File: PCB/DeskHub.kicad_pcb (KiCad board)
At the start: 4 copper layers, 212.6 x 108.9 mm, 120 parts, among them J1 USB_A, J2 5V Barrel, J4 USB_A, J5 USB_A, J6 USB_A, J7 USB_A, U1 TUSB4041I, U2 3.3V Reg, U3 1.1V Reg, U4 TPS2001CDGNR, U5 TPS2001CDGNR, U6 TPS2001CDGNR, U7 TPS2001CDGNR, Y1 ECS-240-20-30B-TR

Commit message: space out vias, add stiching vias, remove teardrops
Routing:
- net BOARD_3.3V: track 4.62 -> 7.07 mm, vias 42 -> 23
- net /Port 3 Power Switch/OVERCURRENT: track 80.4 -> 79.7 mm
- net VDD3.3: vias 16 -> 8
- net VDD1.1: vias 19 -> 11
- net Earth: vias 53 -> 99
- net BOARD_5V: vias 36 -> 29
- net /Port 4 Power Switch/VOUT: vias 4 -> 2
- net /Port 3 Power Switch/VOUT: vias 4 -> 2
- net /Port 2 Power Switch/VOUT: vias 4 -> 2
- net /Port 1 Power Switch/VOUT: vias 4 -> 2
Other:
- board text added: "10K 4.7K ..."

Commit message: pcb v2.0 condensed
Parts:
- moved J6 61.8 mm to (187.5, 137.0)
- moved C69 61.8 mm to (199.3, 132.8)
- moved C70 61.8 mm to (198.4, 132.8)
- moved R18 61.8 mm to (197.4, 132.8)
- moved C42 58.7 mm to (187.1, 78.0)
- moved J7 56.3 mm to (123.5, 137.0)
- moved FB7 55.1 mm to (115.3, 127.7)
- moved C74 54.9 mm to (118.1, 128.1), turned to 90 degrees
- moved C49 54.4 mm to (117.0, 117.2)
- moved R11 54.2 mm to (118.0, 119.6)
- moved C48 54.2 mm to (116.7, 125.3)
- moved U4 54.2 mm to (114.5, 121.3)
- moved C71 54.0 mm to (184.0, 128.1)
- moved FB4 53.8 mm to (182.1, 127.8)
- moved J2 53.8 mm to (197.7, 67.2)
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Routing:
- net USB_DN4_D+: track 146.3 -> 65.1 mm
- net USB_DN4_D-: track 146.2 -> 65.1 mm
- net /Port 4 Power Switch/PWRON_EN: track 130.6 -> 65.2 mm
- net /Port 1 Power Switch/OVERCURRENT: track 125.0 -> 60.8 mm
- net /Port 1 Power Switch/PWRON_EN: track 142.3 -> 78.8 mm
- net /Port 4 Power Switch/OVERCURRENT: track 121.4 -> 59.0 mm
- net USB_DN1_D-: track 111.1 -> 63.9 mm
- net USB_DN1_D+: track 111.1 -> 63.9 mm
- net USB_DN3_D-: track 96.7 -> 53.2 mm
- net USB_DN3_D+: track 96.7 -> 53.2 mm
- net /Port 2 Power Switch/OVERCURRENT: track 85.9 -> 48.3 mm
- net /Port 3 Power Switch/PWRON_EN: track 91.9 -> 55.3 mm
- net /Port 3 Power Switch/OVERCURRENT: track 79.7 -> 43.2 mm
- net /Port 2 Power Switch/PWRON_EN: track 98.9 -> 62.4 mm
- net USB_DN2_D-: track 81.8 -> 57.6 mm
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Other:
- board size 212.6 x 108.9 mm -> 94 x 84.2 mm

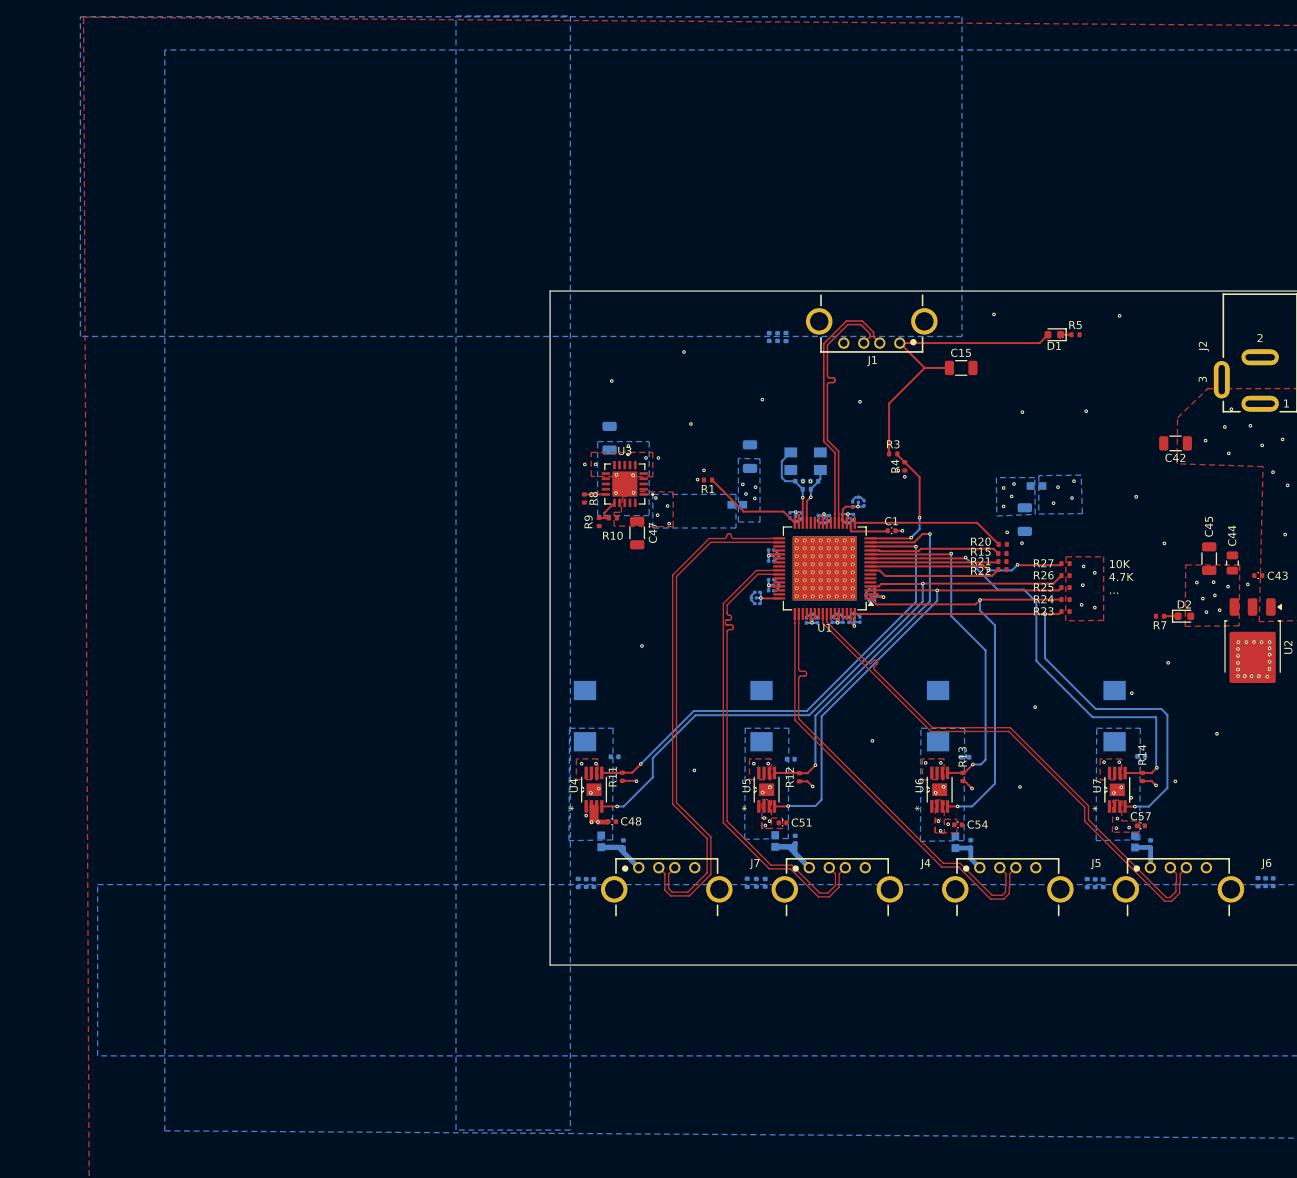
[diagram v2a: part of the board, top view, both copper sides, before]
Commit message: pcb v2.01 reddit review post
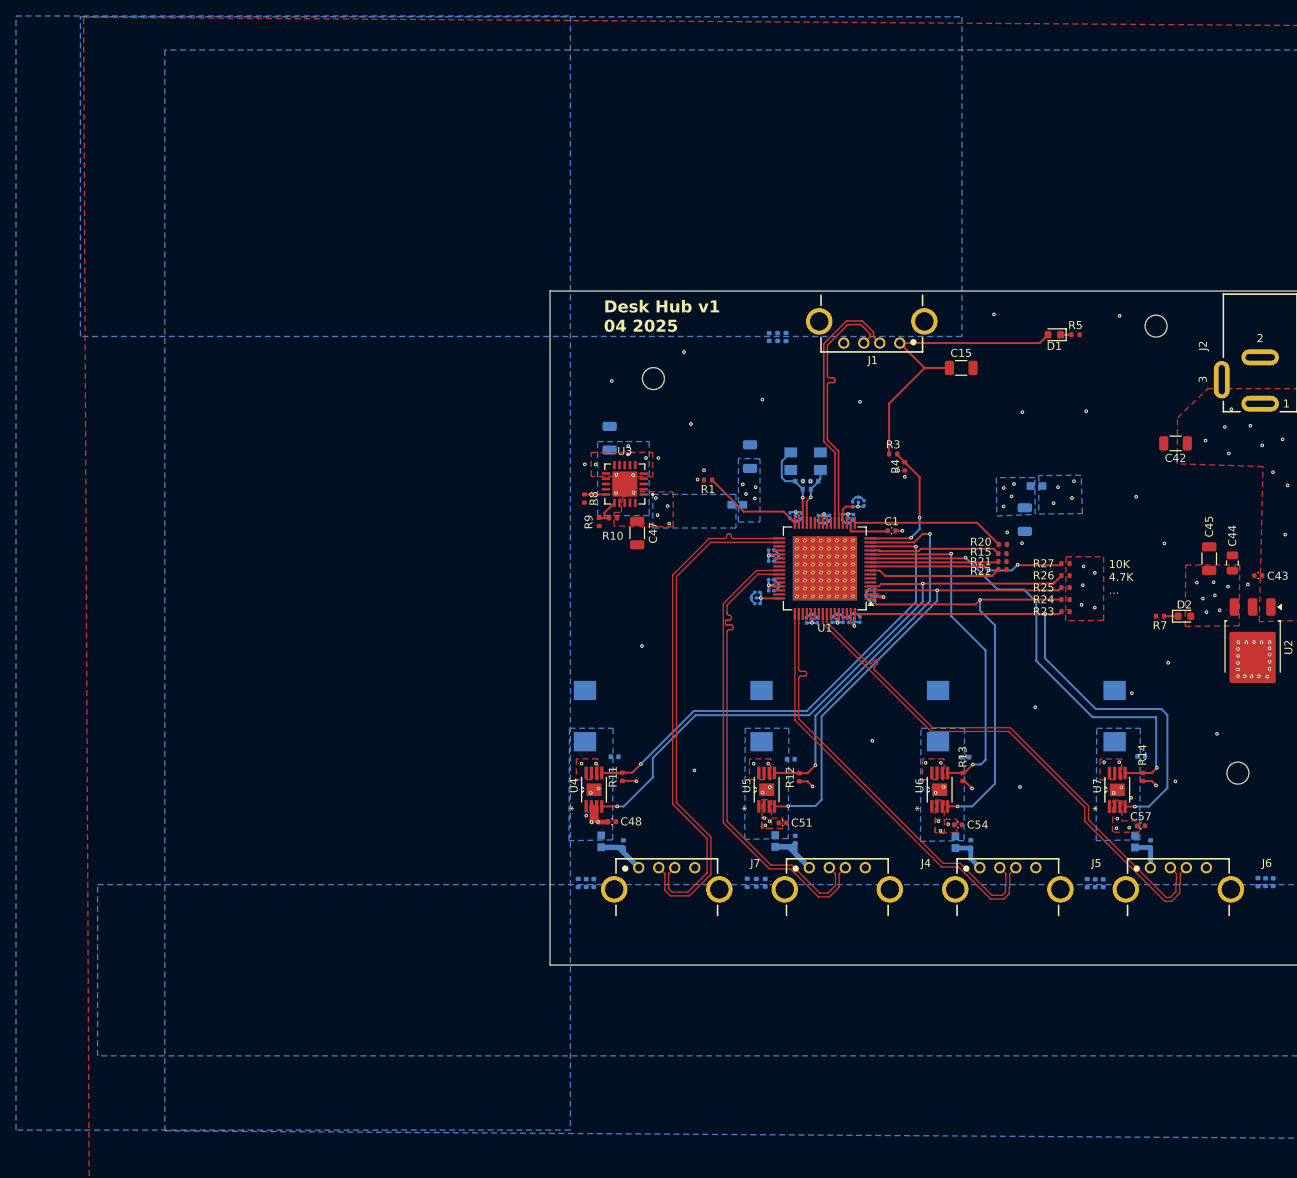
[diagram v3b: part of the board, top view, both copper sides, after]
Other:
- outline, holes or cut-outs redrawn
- board text added: "Desk Hub v1 04 2025"
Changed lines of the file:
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@@
 			(crossoutdnponfab yes)
 			(subtractmaskfromsilk no)
-			(outputformat 1)
+			(outputformat 4)
 			(mirror no)
-			(drillshape 1)
+			(drillshape 0)
 			(scaleselection 1)
 			(outputdirectory "")
@@
 		)
 		(property "Value" "5V Barrel"
-			(at 4.195 12.24 270)
+			(at -2.74 9.395 270)
 			(layer "F.Fab")
 			(effects
@@
 		)
 		(property "Value" "1.1V Reg"
-			(at 9.835 3.885 0)
+			(at 4.55 5.15 0)
 			(layer "F.Fab")
 			(effects
@@
 		(layer "B.SilkS")
 	)
+	(gr_circle
+		(center 121.875 69.875)
+		(end 123.25 69.875)
+		(stroke
+			(width 0.1)
+			(type solid)
+		)
+		(fill no)
+		(layer "Edge.Cuts")
+	)
+	(gr_circle
+		(center 184.714513 63.314514)
+		(end 186.089513 63.314514)
+		(stroke
+			(width 0.1)
+			(type solid)
+		)
+		(fill no)
+		(layer "Edge.Cuts")
+	)
+	(gr_circle
+		(center 194.939513 119.189514)
+		(end 196.314513 119.189514)
+		(stroke
+			(width 0.1)
+			(type solid)
+		)
+		(fill no)
+		(layer "Edge.Cuts")
+	)
 	(gr_rect
 		(start 108.965 58.93)
@@
 		)
 	)
+	(gr_text "Desk Hub v1\n04 2025"
+		(at 115.675 64.2 0)
+		(layer "F.SilkS")
+		(effects
+			(font
+				(size 1.5 1.5)
+				(thickness 0.3)
+				(bold yes)
+			)
+			(justify left bottom)
+		)
+	)
 	(segment
 		(start 152.13 88.9)
@@
 	)
 	(zone
+		(net 0)
+		(net_name "")
+		(layers "F.Cu" "B.Cu" "In1.Cu" "In2.Cu")
+		(name "Keep Out")
+		(hatch edge 0.5)
+		(connect_pads
+			(clearance 0)
+		)
+		(min_thickness 0.25)
+		(filled_areas_thickness no)
+		(keepout
+			(tracks not_allowed)
+			(vias not_allowed)
+			(pads not_allowed)
+			(copperpour not_allowed)
+			(footprints not_allowed)
+		)
+		(placement
+			(enabled no)
+			(sheetname "/")
+		)
+		(fill
+			(thermal_gap 0.5)
+			(thermal_bridge_width 0.5)
+		)
+		(polygon
+			(pts
+				(xy 186.585498 63.191883) (xy 186.553485 62.94872) (xy 186.490007 62.711815) (xy 186.396149 62.485223)
+				(xy 186.273519 62.27282) (xy 186.124213 62.078241) (xy 185.950786 61.904814) (xy 185.756207 61.755508)
+				(xy 185.543804 61.632878) (xy 185.317212 61.53902) (xy 185.080307 61.475542) (xy 184.837144 61.443529)
+				(xy 184.591882 61.443529) (xy 184.348719 61.475542) (xy 184.111814 61.53902) (xy 183.885222 61.632878)
+				(xy 183.672819 61.755508) (xy 183.47824 61.904814) (xy 183.304813 62.078241) (xy 183.155507 62.27282)
+				(xy 183.032877 62.485223) (xy 182.939019 62.711815) (xy 182.875541 62.94872) (xy 182.843528 63.191883)
+				(xy 182.843528 63.437145) (xy 182.875541 63.680308) (xy 182.939019 63.917213) (xy 183.032877 64.143805)
+				(xy 183.155507 64.356208) (xy 183.304813 64.550787) (xy 183.47824 64.724214) (xy 183.672819 64.87352)
+				(xy 183.885222 64.99615) (xy 184.111814 65.090008) (xy 184.348719 65.153486) (xy 184.591882 65.185499)
+				(xy 184.837144 65.185499) (xy 185.080307 65.153486) (xy 185.317212 65.090008) (xy 185.543804 64.99615)
+				(xy 185.756207 64.87352) (xy 185.950786 64.724214) (xy 186.124213 64.550787) (xy 186.273519 64.356208)
+				(xy 186.396149 64.143805) (xy 186.490007 63.917213) (xy 186.553485 63.680308) (xy 186.585498 63.437145)
+			)
+		)
+	)
+	(zone
+		(net 0)
+		(net_name "")
+		(layers "F.Cu" "B.Cu" "In1.Cu" "In2.Cu")
+		(name "Keep Out")
+		(hatch edge 0.5)
+		(connect_pads
+			(clearance 0)
+		)
+		(min_thickness 0.25)
+		(filled_areas_thickness no)
+		(keepout
+			(tracks not_allowed)
+			(vias not_allowed)
+			(pads not_allowed)
+			(copperpour not_allowed)
+			(footprints not_allowed)
+		)
+		(placement
+			(enabled no)
+			(sheetname "/")
+		)
+		(fill
+			(thermal_gap 0.5)
+			(thermal_bridge_width 0.5)
+		)
+		(polygon
+			(pts
+				(xy 123.745985 69.752369) (xy 123.713972 69.509206) (xy 123.650494 69.272301) (xy 123.556636 69.045709)
+				(xy 123.434006 68.833306) (xy 123.2847 68.638727) (xy 123.111273 68.4653) (xy 122.916694 68.315994)
+				(xy 122.704291 68.193364) (xy 122.477699 68.099506) (xy 122.240794 68.036028) (xy 121.997631 68.004015)
+				(xy 121.752369 68.004015) (xy 121.509206 68.036028) (xy 121.272301 68.099506) (xy 121.045709 68.193364)
+				(xy 120.833306 68.315994) (xy 120.638727 68.4653) (xy 120.4653 68.638727) (xy 120.315994 68.833306)
+				(xy 120.193364 69.045709) (xy 120.099506 69.272301) (xy 120.036028 69.509206) (xy 120.004015 69.752369)
+				(xy 120.004015 69.997631) (xy 120.036028 70.240794) (xy 120.099506 70.477699) (xy 120.193364 70.704291)
+				(xy 120.315994 70.916694) (xy 120.4653 71.111273) (xy 120.638727 71.2847) (xy 120.833306 71.434006)
+				(xy 121.045709 71.556636) (xy 121.272301 71.650494) (xy 121.509206 71.713972) (xy 121.752369 71.745985)
+				(xy 121.997631 71.745985) (xy 122.240794 71.713972) (xy 122.477699 71.650494) (xy 122.704291 71.556636)
+				(xy 122.916694 71.434006) (xy 123.111273 71.2847) (xy 123.2847 71.111273) (xy 123.434006 70.916694)
+				(xy 123.556636 70.704291) (xy 123.650494 70.477699) (xy 123.713972 70.240794) (xy 123.745985 69.997631)
+			)
+		)
+	)
+	(zone
+		(net 0)
+		(net_name "")
+		(layers "F.Cu" "B.Cu" "In1.Cu" "In2.Cu")
+		(name "Keep Out")
+		(hatch edge 0.5)
+		(connect_pads
+			(clearance 0)
+		)
+		(min_thickness 0.25)
+		(filled_areas_thickness no)
+		(keepout
+			(tracks not_allowed)
+			(vias not_allowed)
+			(pads not_allowed)
+			(copperpour not_allowed)
+			(footprints not_allowed)
+		)
+		(placement
+			(enabled no)
+			(sheetname "/")
+		)
+		(fill
+			(thermal_gap 0.5)
+			(thermal_bridge_width 0.5)
+		)
+		(polygon
+			(pts
+				(xy 196.810498 119.066883) (xy 196.778485 118.82372) (xy 196.715007 118.586815) (xy 196.621149 118.360223)
+				(xy 196.498519 118.14782) (xy 196.349213 117.953241) (xy 196.175786 117.779814) (xy 195.981207 117.630508)
+				(xy 195.768804 117.507878) (xy 195.542212 117.41402) (xy 195.305307 117.350542) (xy 195.062144 117.318529)
+				(xy 194.816882 117.318529) (xy 194.573719 117.350542) (xy 194.336814 117.41402) (xy 194.110222 117.507878)
+				(xy 193.897819 117.630508) (xy 193.70324 117.779814) (xy 193.529813 117.953241) (xy 193.380507 118.14782)
+				(xy 193.257877 118.360223) (xy 193.164019 118.586815) (xy 193.100541 118.82372) (xy 193.068528 119.066883)
+				(xy 193.068528 119.312145) (xy 193.100541 119.555308) (xy 193.164019 119.792213) (xy 193.257877 120.018805)
+				(xy 193.380507 120.231208) (xy 193.529813 120.425787) (xy 193.70324 120.599214) (xy 193.897819 120.74852)
+				(xy 194.110222 120.87115) (xy 194.336814 120.965008) (xy 194.573719 121.028486) (xy 194.816882 121.060499)
+				(xy 195.062144 121.060499) (xy 195.305307 121.028486) (xy 195.542212 120.965008) (xy 195.768804 120.87115)
+				(xy 195.981207 120.74852) (xy 196.175786 120.599214) (xy 196.349213 120.425787) (xy 196.498519 120.231208)
+				(xy 196.621149 120.018805) (xy 196.715007 119.792213) (xy 196.778485 119.555308) (xy 196.810498 119.312145)
+			)
+		)
+	)
+	(zone
 		(net 12)
 		(net_name "/Port 1 Power Switch/VOUT")
@@
 		(polygon
 			(pts
-				(xy 97.2 24.55) (xy 111.5 24.55) (xy 111.5 163.808384) (xy 97.2 163.808384)
+				(xy 42.2 24.55) (xy 111.5 24.55) (xy 111.5 163.808384) (xy 42.2 163.808384)
 			)
 		)
@@
 		(polygon
 			(pts
-				(xy 147.6 95.3) (xy 169.85 96.05) (xy 169.45 80.2) (xy 158.25 80.25) (xy 158.2 89.5) (xy 147.55 89.6)
+				(xy 148.4 96) (xy 169.85 96.05) (xy 169.45 80.2) (xy 158.25 80.25) (xy 158.2 89.5) (xy 147.55 89.6)
 			)
 		)

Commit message: work on pcb new power
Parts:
- removed C46: 10uF, Capacitor_SMD:C_1206_3216Metric
- removed D2: LED Green, LED_SMD:LED_0603_1608Metric
- removed R10: 1.87K, my_global:R_0402_1005Metric_1.5mm_silkscreen_clearance
- removed R9: 4.99K, my_global:R_0402_1005Metric_1.5mm_silkscreen_clearance
- added C60: 2.2uF, Capacitor_SMD:C_0805_2012Metric, F.Cu at (220.7, 107.5)
- added C61: 2.2uF, Capacitor_SMD:C_0805_2012Metric, F.Cu at (220.2, 111.3)
- added C62: 2.2uF, Capacitor_SMD:C_0805_2012Metric, F.Cu at (243.8, 112.3)
- added C75: 2.2uF, Capacitor_SMD:C_0805_2012Metric, F.Cu at (244.6, 108.5)
- added C76: 22uF, Capacitor_SMD:C_0201_0603Metric, F.Cu at (191.5, 83.1)
- added L1: 3.3uH, my_global:NRS5030T3R3MMGJ, F.Cu at (195.5, 86.2)
- added R28: 10K, Resistor_SMD:R_0402_1005Metric, F.Cu at (238.2, 106.3)
- added R29: 10K, Resistor_SMD:R_0402_1005Metric, F.Cu at (238.2, 108.3)
- added R30: 50K, Resistor_SMD:R_0402_1005Metric, F.Cu at (238.2, 110.3)
- added R31: 10K, Resistor_SMD:R_0402_1005Metric, F.Cu at (238.2, 112.3)
- C1, C13, C14, C16, C17, C48, C49, C51, C52, C54, C55, C57, C58, C63, C64, C65, C66, C67, C68, C69, C70, C71, C72, C73, C74: footprint my_global:C_0402_1005Metric_1.5mm_silkscreen_clearance -> Capacitor_SMD:C_0402_1005Metric
- C43: value 1uF -> 100uF; footprint my_global:C_0402_1005Metric_1.5mm_silkscreen_clearance -> Capacitor_SMD:CP_Elec_6.3x7.7
- C44: value 2.2uF -> 10uF; footprint Capacitor_SMD:C_0805_2012Metric -> Capacitor_SMD:C_1206_3216Metric
- C45: value 10uF -> 0.1uF; footprint Capacitor_SMD:C_1206_3216Metric -> Capacitor_SMD:C_0402_1005Metric
- C47: value 10uF -> 22uF; footprint Capacitor_SMD:C_1206_3216Metric -> Capacitor_SMD:C_0201_0603Metric
- J2: value 5V Barrel -> 7.5V Barrel
- R1, R11, R12, R13, R14, R15, R16, R17, R18, R19, R2, R20, R21, R22, R23, R24, R25, R26, R27, R3, R4, R5, R6: footprint my_global:R_0402_1005Metric_1.5mm_silkscreen_clearance -> Resistor_SMD:R_0402_1005Metric
- R7: value 330 -> 52.3k; footprint my_global:R_0402_1005Metric_1.5mm_silkscreen_clearance -> Resistor_SMD:R_0402_1005Metric
- R8: value 10K -> 10k; footprint my_global:R_0402_1005Metric_1.5mm_silkscreen_clearance -> Resistor_SMD:R_0402_1005Metric
- U2: value 3.3V Reg -> Switching 5V Regulator; footprint Package_TO_SOT_SMD:TO-252-3_TabPin2 -> Package_TO_SOT_SMD:SOT-563
- U3: value 1.1V Reg -> Dual LDO; footprint my_global:QFN65P500X500X100-21N -> my_global:SON_1PDSQR_TEX
- moved R8 84.7 mm to (197.8, 80.0), turned to 180 degrees
- moved U3 75.1 mm to (192.1, 97.0), turned to -90 degrees
- moved C47 70.9 mm to (190.5, 83.1), turned to 90 degrees
- moved C42 24.7 mm to (207.7, 91.7)
- moved R7 23.4 mm to (200.2, 81.6)
- moved U2 21.3 mm to (197.6, 82.2), turned to 0 degrees
- moved C43 20.8 mm to (187.8, 76.1)
- moved C44 14.2 mm to (186.3, 81.1), turned to 180 degrees
- moved C45 12.1 mm to (199.3, 83.3)
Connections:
- net XI renamed Net-(U1-XI)
- net XO renamed Net-(U1-XO)
- C43 pad 1: BOARD_5V -> VIN
- C44 pad 1: BOARD_3.3V -> VIN
- C45 pad 1: BOARD_3.3V -> Net-(U2-SW)
- C45 pad 2: Earth -> Net-(U2-BST)
- C47 pad 1: BOARD_1.1V -> BOARD_5V
- J2 pad 1: BOARD_5V -> VIN
- R7 pad 1: Net-(D2-K) -> BOARD_5V
- R7 pad 2: Earth -> Net-(U2-FB)
- R8 pad 1: Net-(U3-SS) -> Net-(U2-FB)
- U2 pad 1: BOARD_5V -> VIN
- U2 pad 2: Earth -> Net-(U2-SW)
- U2 pad 3: BOARD_3.3V -> Earth
- U3 pad 1: BOARD_1.1V -> Net-(U3-FB1)
- U3 pad 10: BOARD_3.3V -> BOARD_1.1V
- U3 pad 11: BOARD_3.3V -> Earth
- U3 pad 2: unconnected-(U3-NC_2-Pad2) -> Earth
- U3 pad 3: unconnected-(U3-NC_3-Pad3) -> BOARD_5V
- U3 pad 4: unconnected-(U3-NC_4-Pad4) -> Earth
- U3 pad 5: BOARD_3.3V -> BOARD_5V
- U3 pad 6: BOARD_3.3V -> BOARD_5V
- U3 pad 7: BOARD_3.3V -> Net-(U3-FB2)
- U3 pad 9: unconnected-(U3-PG-Pad9) -> BOARD_5V
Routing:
- net BOARD_5V: track 5.31 -> 16.7 mm, vias 20 -> 17
- net (no net): track 0.00 -> 6.15 mm
- net Net-(U3-FB): track 3.46 -> 0.00 mm
- net Net-(U3-SS): track 2.69 -> 0.00 mm
- net Net-(D2-K): track 1.75 -> 0.00 mm
- net Net-(U2-BST): track 0.00 -> 1.00 mm
- net Earth: vias 66 -> 46
- net BOARD_3.3V: vias 23 -> 16
- added copper zone on F.Cu, net Net-(U2-FB)
- added copper zone on F.Cu, net Net-(U2-SW)
- added copper zone on F.Cu, net VIN
